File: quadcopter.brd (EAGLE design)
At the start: 76 x 76 mm, 69 parts, among them J1 AVR_SPI_PRG_6NS, U1 ATMEGA128RFA1, Y2 16MHz

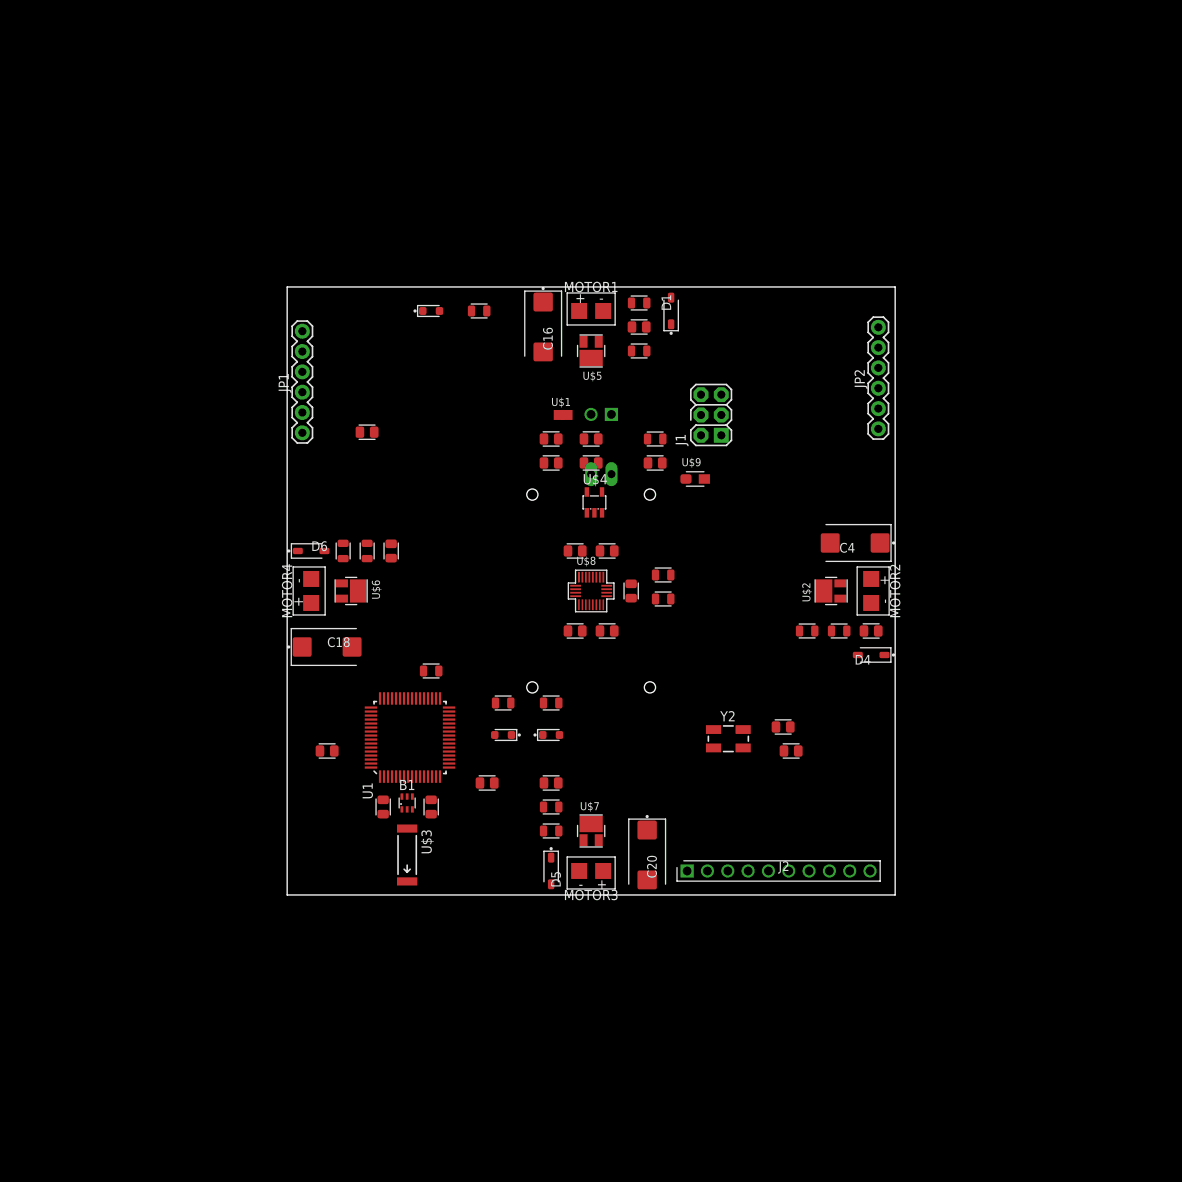
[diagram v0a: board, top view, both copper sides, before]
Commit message: AO: adding redesigned board with X configuration
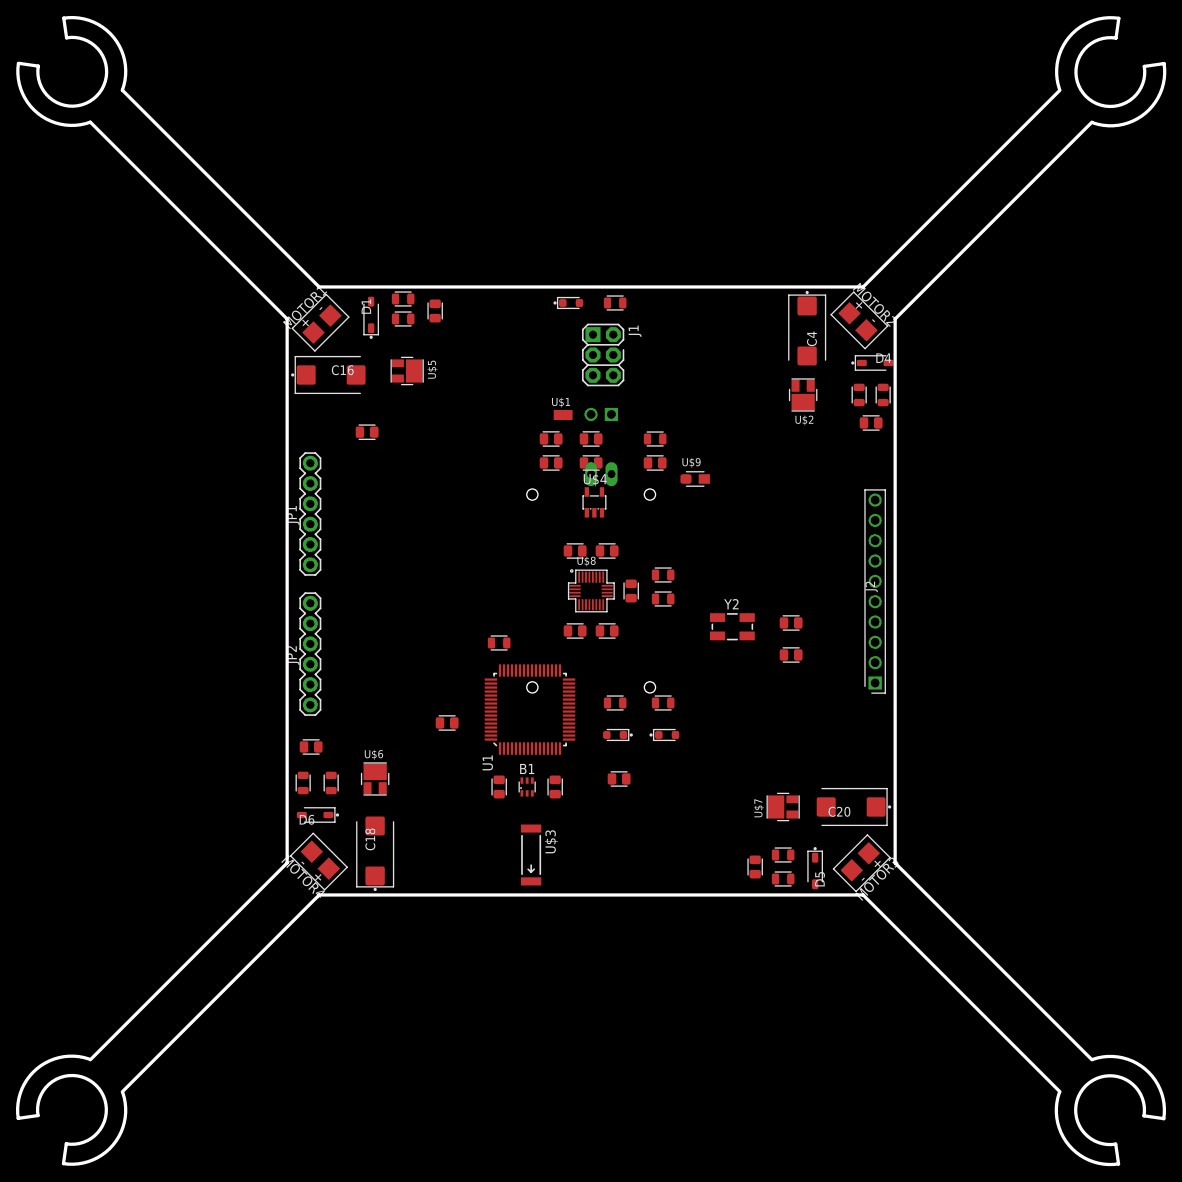
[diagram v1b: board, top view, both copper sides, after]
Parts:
- C1, C15, C17, C19: value 1uF -> 0.1uF
- moved JP2 78.9 mm to (2.90, 23.8)
- moved D1 37.5 mm to (10.5, 72.5)
- moved D4 36.5 mm to (73.5, 66.5), turned to 0 degrees
- moved MOTOR1 33.6 mm to (4.00, 71.0), turned to 45 degrees
- moved MOTOR2 33.6 mm to (71.0, 72.0), turned to 315 degrees
- moved MOTOR3 33.5 mm to (72.0, 4.50), turned to 225 degrees
- moved MOTOR4 33.5 mm to (4.50, 4.00), turned to 135 degrees
- moved J2 33.2 mm to (73.5, 26.5), turned to 90 degrees
- moved D6 33.0 mm to (3.50, 10.0), turned to 180 degrees
- moved D5 33.0 mm to (66.0, 3.00)
- moved R1 31.0 mm to (74.5, 62.5), turned to 90 degrees
- moved R10 30.4 mm to (62.0, 2.00)
- moved R6 30.2 mm to (14.5, 74.5), turned to 180 degrees
- moved R8 30.1 mm to (2.00, 14.0)
- moved R2 29.6 mm to (71.5, 62.5), turned to 90 degrees
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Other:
- board size 76 x 76 mm -> 143.4 x 143.4 mm

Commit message: added the ground and power planes to the board as well as the Ground Shield/Faraday cage to the antenna but may need review
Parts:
- moved C10 0.60 mm to (27.1, 13.5)
- moved U$3 0.50 mm to (30.0, 5.00)
- moved B1 0.30 mm to (30.3, 13.5), turned to 90 degrees
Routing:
- added copper zone on layer 15, net 3V
- added copper zone on layer 2, net BAT_GND
- added copper zone on layer 1, net GND
- added copper zone on layer 2, net GND
- added copper zone on layer 15, net VBAT

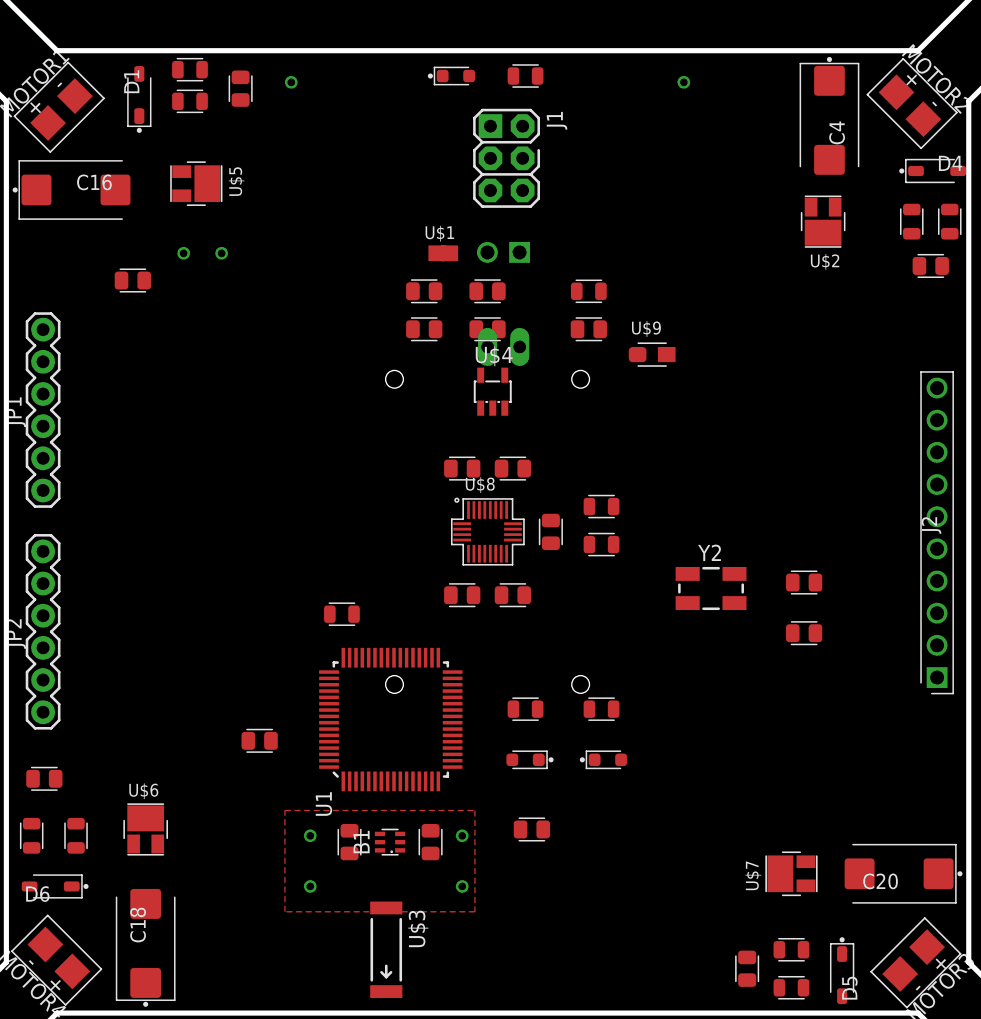
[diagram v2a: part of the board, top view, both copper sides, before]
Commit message: Fixed small issues in schematic, worked on board layout (antenna and pour connections mostly)
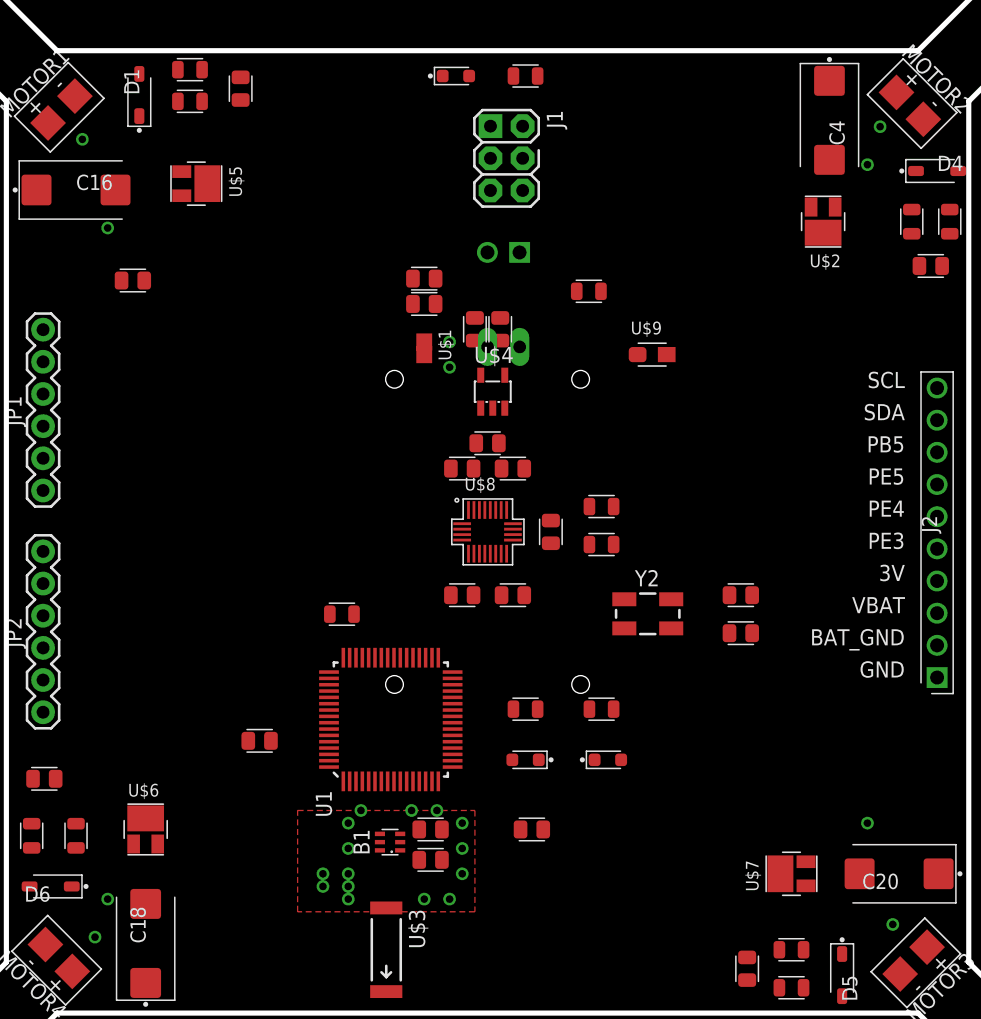
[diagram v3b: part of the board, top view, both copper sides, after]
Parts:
- moved C2 9.00 mm to (38.0, 45.0)
- moved C3 9.00 mm to (37.0, 54.0), turned to 270 degrees
- moved U$1 7.07 mm to (33.0, 53.0), turned to 270 degrees
- moved C10 6.55 mm to (33.5, 12.1), turned to 180 degrees
- moved Y2 5.39 mm to (50.6, 31.5)
- moved C5 5.10 mm to (58.0, 33.0)
- moved C6 5.00 mm to (58.0, 30.0)
- moved C14 3.16 mm to (39.0, 54.0), turned to 90 degrees
- moved C11 2.00 mm to (33.0, 56.0)
- moved C12 1.00 mm to (33.0, 58.0)
- moved C9 1.00 mm to (33.5, 14.5), turned to 0 degrees
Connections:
- removed net A0: U1.63
- removed net A1: U1.64
- removed net A2: U1.1
- removed net A3: U1.2
- removed net A4: U1.3
- removed net A5: U1.4
- removed net A6: U1.5
- removed net A7: U1.6
- removed net AREF: U1.62
- removed net PD4: U1.29
- removed net PD5: U1.30
- removed net PD6: U1.31
- removed net PD7: U1.32
- removed net PE2: U1.48
- removed net PE6: U1.52
- removed net PE7: U1.53
- removed net PG0: U1.14
- removed net PG1: U1.15
- removed net PG2: U1.16
- removed net PG3: U1.17
- removed net PG4: U1.18
- removed net PG5: U1.19
- removed net RSTON: U1.13
- removed net SSN: U1.36
- net BAT_GND: now also BATT1.-
- net GND: no longer BATT1.-

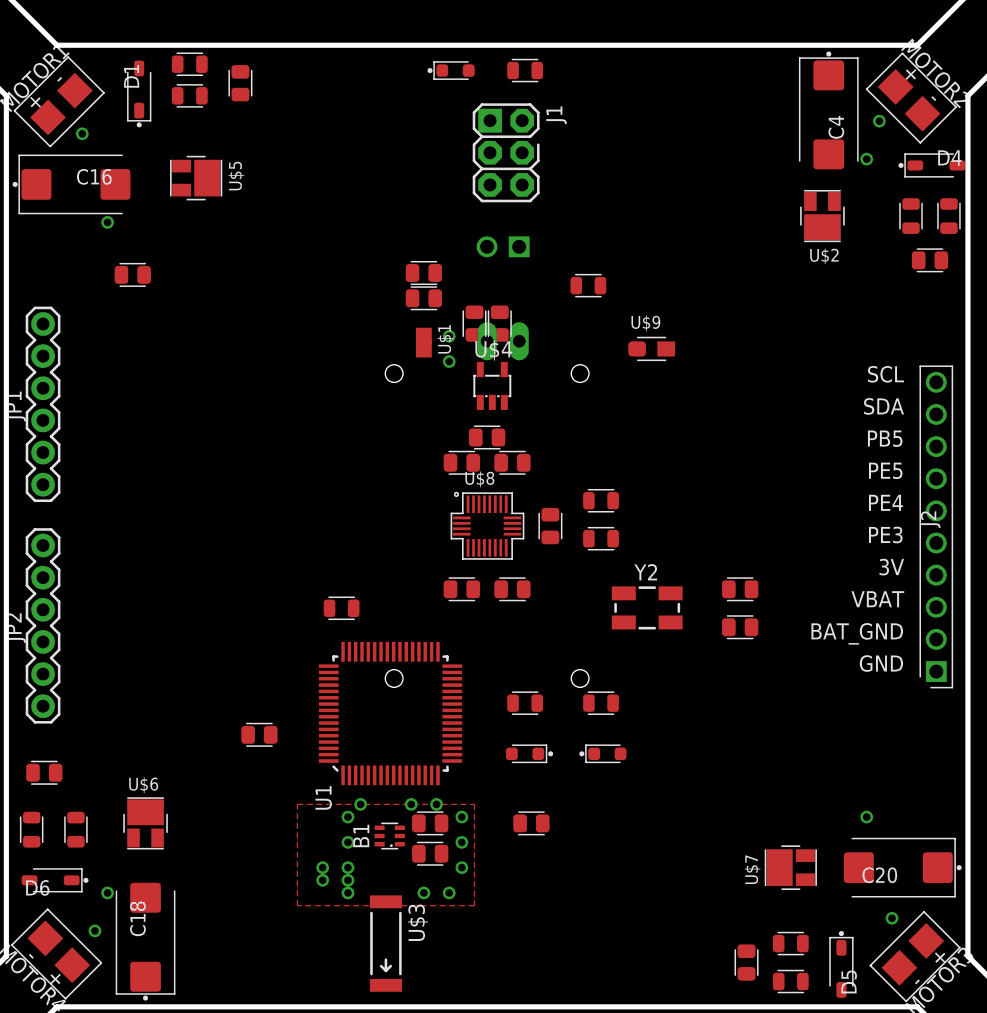
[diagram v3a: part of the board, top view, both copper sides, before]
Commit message: Board optimizations, focusing on IMU and making space for the autorouter.
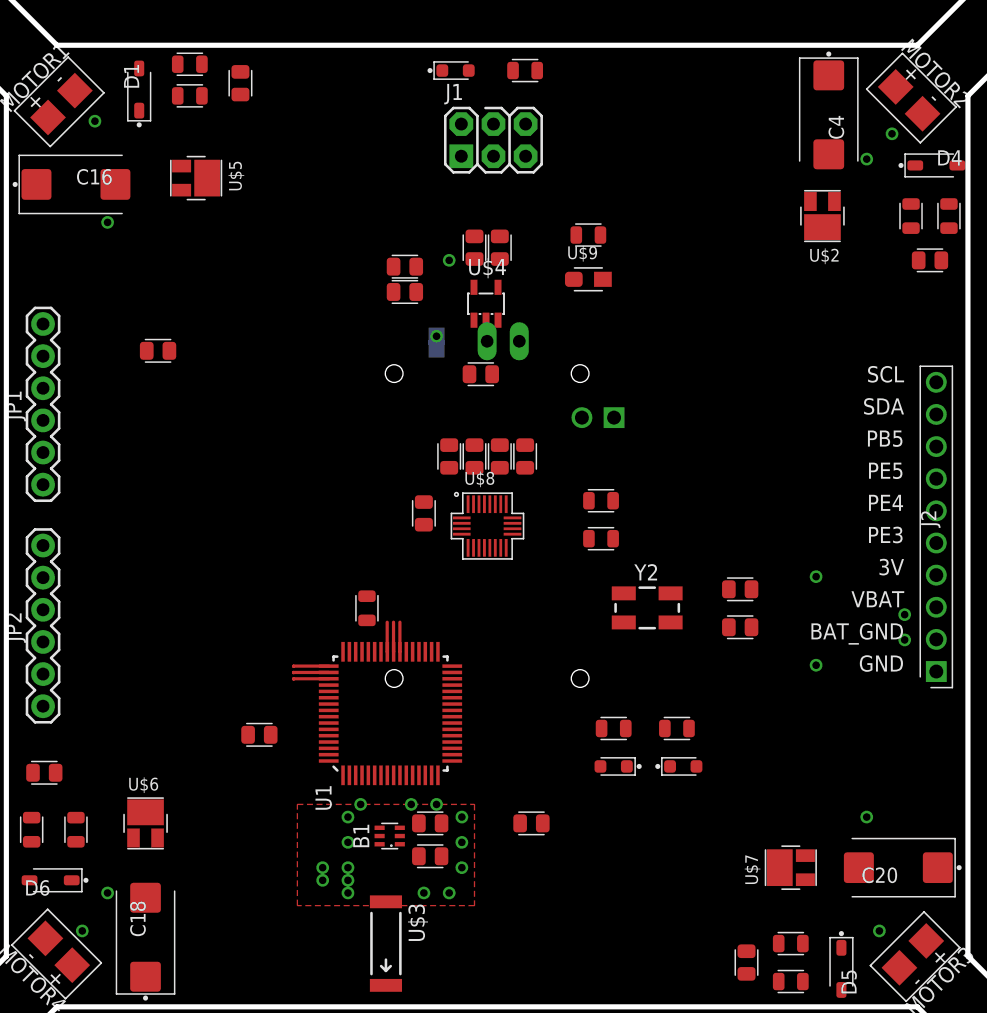
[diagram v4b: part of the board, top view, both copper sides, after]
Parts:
- moved J3 15.4 mm to (48.0, 46.6)
- moved C24 10.5 mm to (37.0, 43.5), turned to 90 degrees
- moved C21 9.22 mm to (33.0, 39.0), turned to 90 degrees
- moved U$9 7.43 mm to (46.0, 57.5)
- moved R4 7.28 mm to (48.0, 22.0)
- moved D3 7.07 mm to (48.0, 19.0)
- moved C23 6.80 mm to (39.0, 43.5)
- moved U$4 6.52 mm to (37.9, 55.6)
- moved C13 6.32 mm to (12.0, 51.9)
- moved R14 6.32 mm to (53.0, 22.0)
- moved D7 6.08 mm to (53.5, 19.0)
- moved C14 6.00 mm to (39.0, 60.0)
- moved C3 6.00 mm to (37.0, 60.0)
- moved C2 5.02 mm to (37.5, 50.0)
- moved R15 4.00 mm to (46.0, 61.0)
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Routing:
- net PE5: track 0.00 -> 2.81 mm
- net PE4: track 0.00 -> 2.81 mm
- net PE3: track 0.00 -> 2.81 mm
- net PB5: track 0.00 -> 2.35 mm
- net PB4: track 0.00 -> 2.35 mm
- net MISO: track 0.00 -> 2.34 mm
- added copper zone on layer 15, net N$14
